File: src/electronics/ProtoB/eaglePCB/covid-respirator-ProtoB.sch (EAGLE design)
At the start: 49 parts, among them IC1 AD825R, IC2 L7805CV-DG, IC3 AD8607R, IC4 AD8607R, T2 BC548

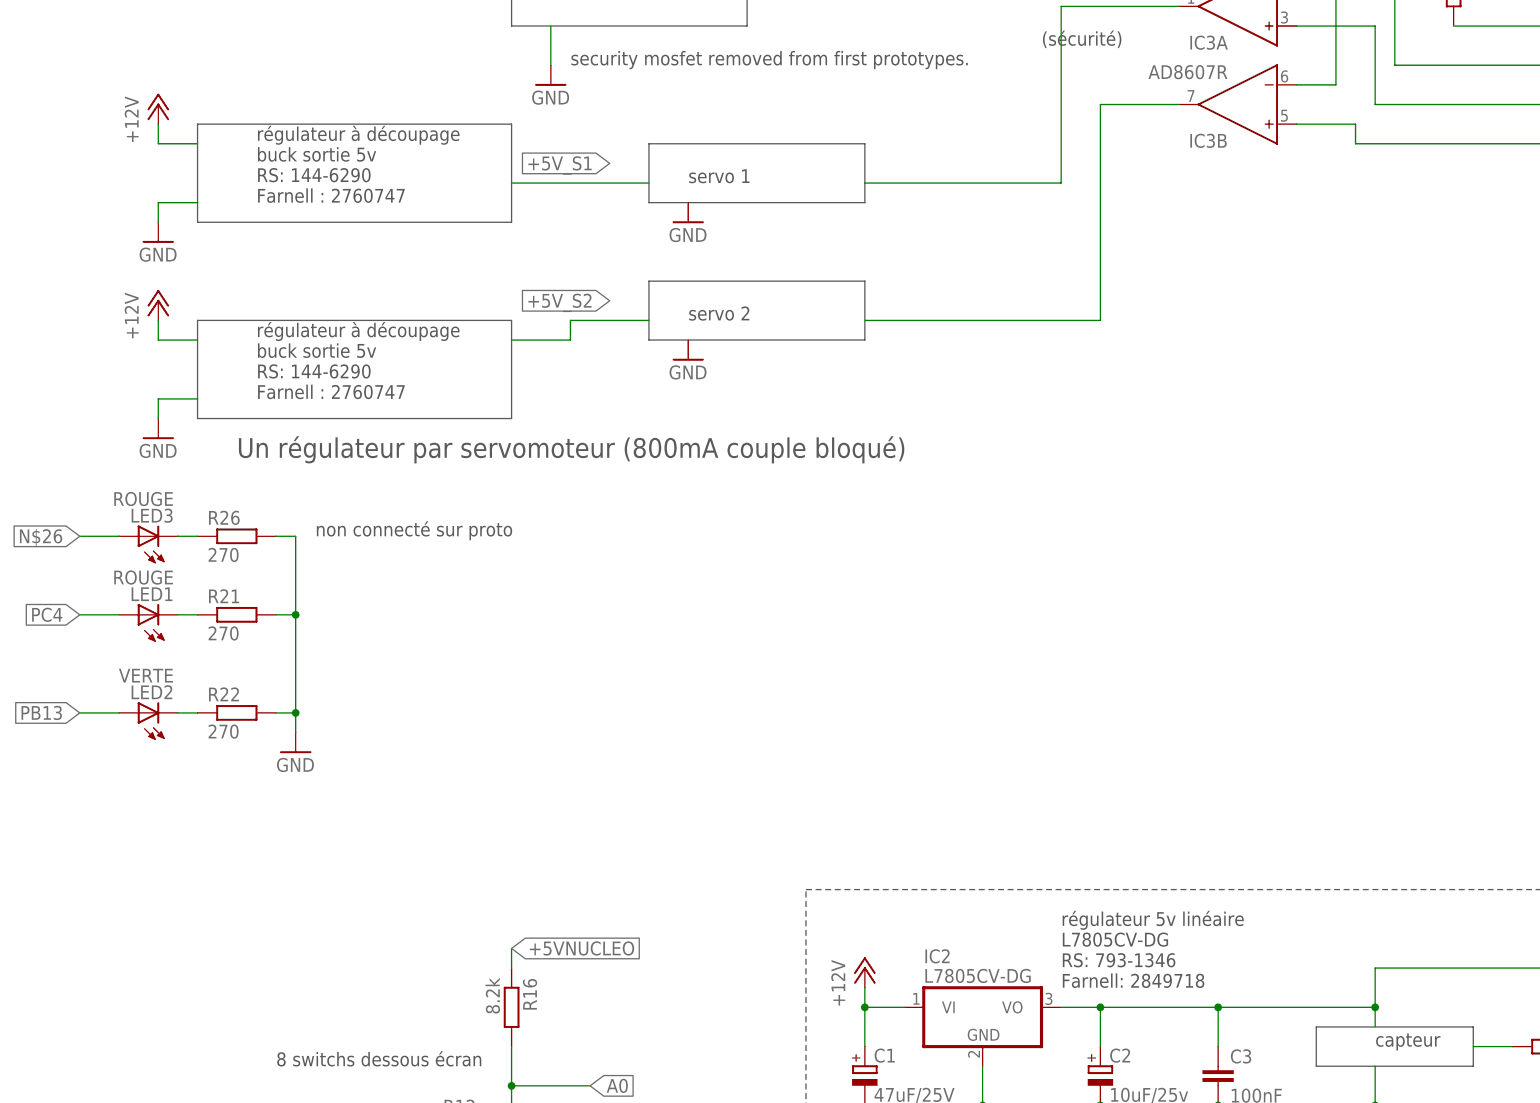
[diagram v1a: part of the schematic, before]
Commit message: update protoB schematic
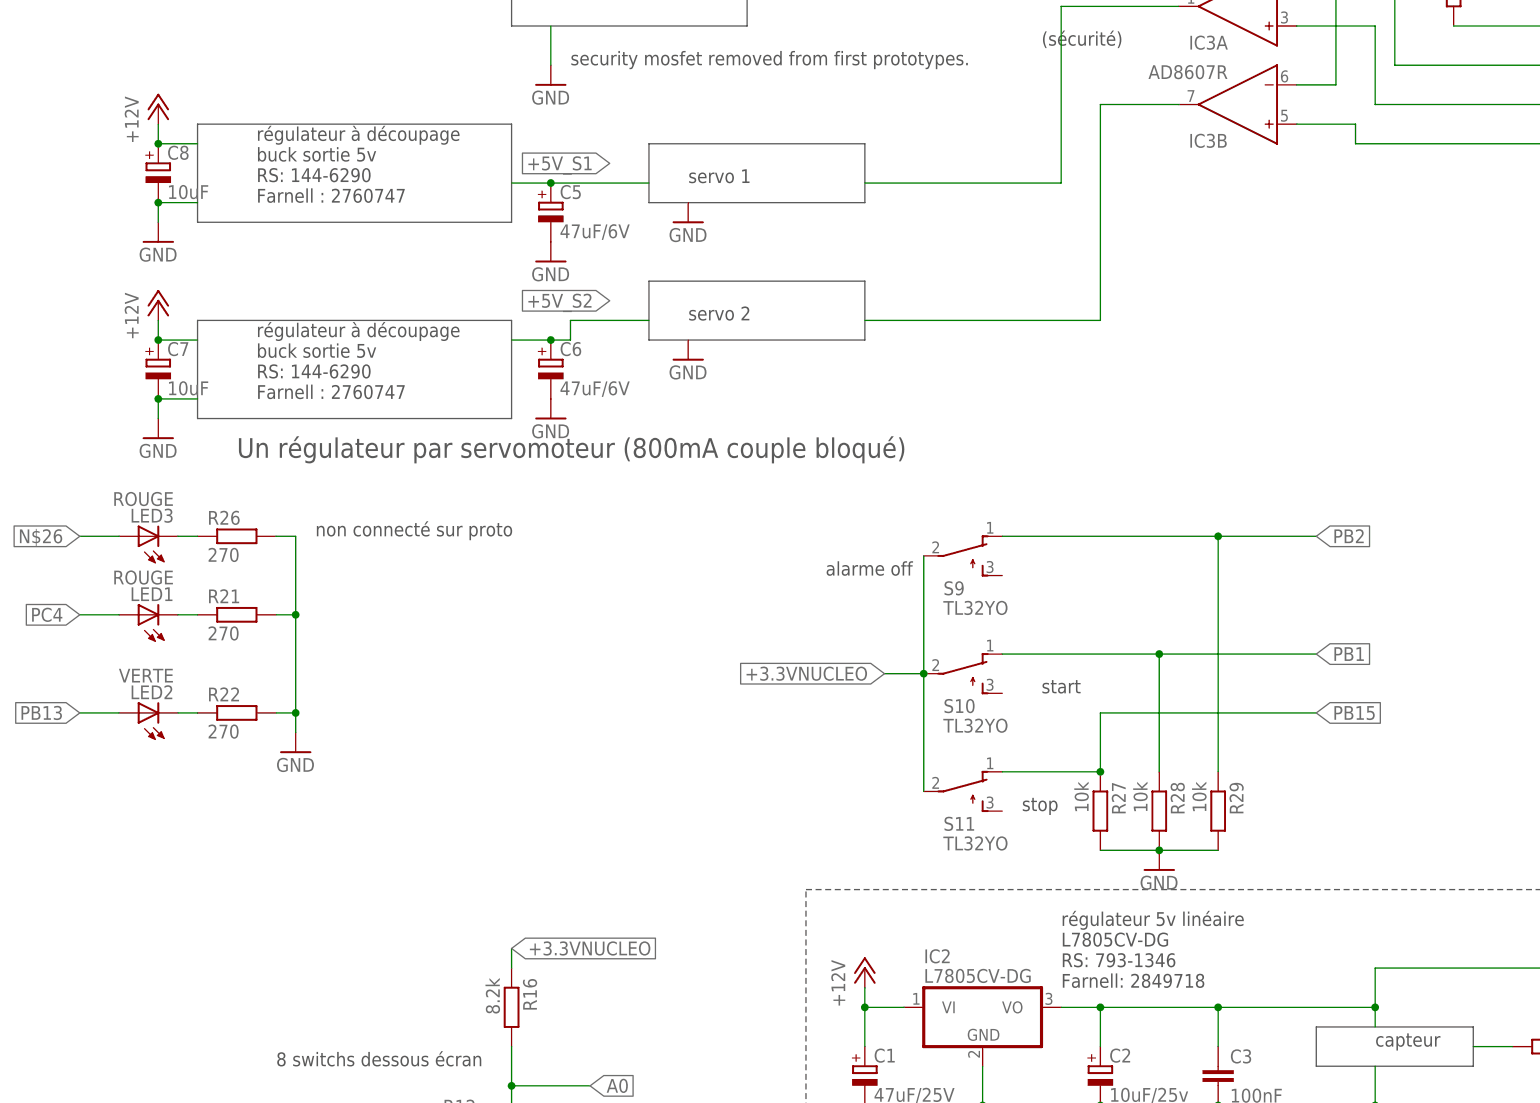
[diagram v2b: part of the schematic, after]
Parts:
- added C5, C6: 47uF/6V, rcl:CPOL-EU150CLZ-1010
- added C7, C8: 10uF, rcl:CPOL-EU150CLZ-1010
- added R27, R28, R29: 10k, rcl:R-EU_0207/10
- added S10, S11, S9: TL32YO, switch:TL32YO
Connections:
- new net +3.3VNUCLEO: R16.1, S10.P, S11.P, S9.P
- new net +5V_S1: C5.+
- new net +5V_S2: C6.+
- new net PB1: R28.1, S10.O
- new net PB15: R27.1, S11.O
- new net PB2: R29.1, S9.O
- net +12V: now also C7.+, C8.+
- net +5VNUCLEO: no longer R16.1
- net GND: now also C5.-, C6.-, C7.-, C8.-, R27.2, R28.2, R29.2
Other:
- note added: "alarme off"
- note added: "start"
- note added: "stop"
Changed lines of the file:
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@@
 <part name="LED3" library="led" deviceset="LED" device="3MM" value="ROUGE"/>
 <part name="R26" library="rcl" deviceset="R-EU_" device="0207/10" value="270"/>
+<part name="C5" library="rcl" deviceset="CPOL-EU" device="150CLZ-1010" value="47uF/6V"/>
+<part name="C6" library="rcl" deviceset="CPOL-EU" device="150CLZ-1010" value="47uF/6V"/>
+<part name="GND16" library="supply1" deviceset="GND" device=""/>
+<part name="GND17" library="supply1" deviceset="GND" device=""/>
+<part name="C7" library="rcl" deviceset="CPOL-EU" device="150CLZ-1010" value="10uF"/>
+<part name="C8" library="rcl" deviceset="CPOL-EU" device="150CLZ-1010" value="10uF"/>
+<part name="S9" library="switch" deviceset="TL32YO" device=""/>
+<part name="S10" library="switch" deviceset="TL32YO" device=""/>
+<part name="S11" library="switch" deviceset="TL32YO" device=""/>
+<part name="R27" library="rcl" deviceset="R-EU_" device="0207/10" value="10k"/>
+<part name="R28" library="rcl" deviceset="R-EU_" device="0207/10" value="10k"/>
+<part name="R29" library="rcl" deviceset="R-EU_" device="0207/10" value="10k"/>
+<part name="GND18" library="supply1" deviceset="GND" device=""/>
 </parts>
 <sheets>
@@
 pour un pont diviseur fixé</text>
 <text x="58.42" y="35.56" size="1.778" layer="97">non connecté sur proto</text>
+<text x="124.46" y="30.48" size="1.778" layer="97">alarme off</text>
+<text x="152.4" y="15.24" size="1.778" layer="97">start</text>
+<text x="149.86" y="0" size="1.778" layer="97">stop</text>
 </plain>
 <instances>
@@
 <instance part="LED3" gate="G$1" x="35.56" y="35.56" rot="R90"/>
 <instance part="R26" gate="G$1" x="48.26" y="35.56"/>
+<instance part="C5" gate="G$1" x="88.9" y="78.74"/>
+<instance part="C6" gate="G$1" x="88.9" y="58.42"/>
+<instance part="GND16" gate="1" x="88.9" y="50.8"/>
+<instance part="GND17" gate="1" x="88.9" y="71.12"/>
+<instance part="C7" gate="G$1" x="38.1" y="58.42"/>
+<instance part="C8" gate="G$1" x="38.1" y="83.82"/>
+<instance part="S9" gate="BEF1" x="142.24" y="33.02" rot="R270"/>
+<instance part="S10" gate="BEF1" x="142.24" y="17.78" rot="R270"/>
+<instance part="S11" gate="BEF1" x="142.24" y="2.54" rot="R270"/>
+<instance part="R27" gate="G$1" x="160.02" y="0" rot="R270"/>
+<instance part="R28" gate="G$1" x="167.64" y="0" rot="R270"/>
+<instance part="R29" gate="G$1" x="175.26" y="0" rot="R270"/>
+<instance part="GND18" gate="1" x="167.64" y="-7.62"/>
 </instances>
 <busses>
@@
 <wire x1="43.18" y1="78.74" x2="38.1" y2="78.74" width="0.1524" layer="91"/>
 <wire x1="38.1" y1="78.74" x2="38.1" y2="76.2" width="0.1524" layer="91"/>
+<pinref part="C8" gate="G$1" pin="-"/>
+<junction x="38.1" y="78.74"/>
 </segment>
 <segment>
@@
 <wire x1="43.18" y1="53.34" x2="38.1" y2="53.34" width="0.1524" layer="91"/>
 <wire x1="38.1" y1="53.34" x2="38.1" y2="50.8" width="0.1524" layer="91"/>
+<pinref part="C7" gate="G$1" pin="-"/>
+<junction x="38.1" y="53.34"/>
 </segment>
 <segment>
@@
 <wire x1="246.38" y1="71.12" x2="246.38" y2="68.58" width="0.1524" layer="91"/>
 </segment>
+<segment>
+<pinref part="C6" gate="G$1" pin="-"/>
+<pinref part="GND16" gate="1" pin="GND"/>
+</segment>
+<segment>
+<pinref part="C5" gate="G$1" pin="-"/>
+<pinref part="GND17" gate="1" pin="GND"/>
+</segment>
+<segment>
+<pinref part="R28" gate="G$1" pin="2"/>
+<pinref part="GND18" gate="1" pin="GND"/>
+<pinref part="R27" gate="G$1" pin="2"/>
+<wire x1="160.02" y1="-5.08" x2="167.64" y2="-5.08" width="0.1524" layer="91"/>
+<junction x="167.64" y="-5.08"/>
+<pinref part="R29" gate="G$1" pin="2"/>
+<wire x1="167.64" y1="-5.08" x2="175.26" y2="-5.08" width="0.1524" layer="91"/>
+</segment>
 </net>
 <net name="+12V" class="0">
@@
 <wire x1="38.1" y1="88.9" x2="38.1" y2="86.36" width="0.1524" layer="91"/>
 <wire x1="38.1" y1="86.36" x2="43.18" y2="86.36" width="0.1524" layer="91"/>
+<pinref part="C8" gate="G$1" pin="+"/>
+<junction x="38.1" y="86.36"/>
 </segment>
 <segment>
@@
 <wire x1="38.1" y1="63.5" x2="38.1" y2="60.96" width="0.1524" layer="91"/>
 <wire x1="38.1" y1="60.96" x2="43.18" y2="60.96" width="0.1524" layer="91"/>
+<pinref part="C7" gate="G$1" pin="+"/>
+<junction x="38.1" y="60.96"/>
 </segment>
 </net>
@@
 <wire x1="101.6" y1="63.5" x2="91.44" y2="63.5" width="0.1524" layer="91"/>
 <wire x1="91.44" y1="63.5" x2="91.44" y2="60.96" width="0.1524" layer="91"/>
-<wire x1="91.44" y1="60.96" x2="83.82" y2="60.96" width="0.1524" layer="91"/>
+<wire x1="91.44" y1="60.96" x2="88.9" y2="60.96" width="0.1524" layer="91"/>
+<pinref part="C6" gate="G$1" pin="+"/>
+<wire x1="88.9" y1="60.96" x2="83.82" y2="60.96" width="0.1524" layer="91"/>
+<junction x="88.9" y="60.96"/>
 </segment>
 </net>
@@
 <segment>
 <label x="96.52" y="83.82" size="1.778" layer="95" rot="R180" xref="yes"/>
-<wire x1="101.6" y1="81.28" x2="83.82" y2="81.28" width="0.1524" layer="91"/>
+<wire x1="101.6" y1="81.28" x2="88.9" y2="81.28" width="0.1524" layer="91"/>
+<pinref part="C5" gate="G$1" pin="+"/>
+<wire x1="88.9" y1="81.28" x2="83.82" y2="81.28" width="0.1524" layer="91"/>
+<junction x="88.9" y="81.28"/>
 </segment>
 </net>
@@
 <wire x1="-22.86" y1="-17.78" x2="-27.94" y2="-17.78" width="0.1524" layer="91"/>
 <junction x="-22.86" y="-17.78"/>
-</segment>
-<segment>
-<pinref part="R16" gate="G$1" pin="1"/>
-<wire x1="83.82" y1="-20.32" x2="83.82" y2="-17.78" width="0.1524" layer="91"/>
-<label x="83.82" y="-17.78" size="1.778" layer="95" xref="yes"/>
 </segment>
 </net>
@@
 </segment>
 </net>
+<net name="PB15" class="0">
+<segment>
+<pinref part="R27" gate="G$1" pin="1"/>
+<pinref part="S11" gate="BEF1" pin="O"/>
+<wire x1="160.02" y1="5.08" x2="147.32" y2="5.08" width="0.1524" layer="91"/>
+<wire x1="160.02" y1="5.08" x2="160.02" y2="12.7" width="0.1524" layer="91"/>
+<junction x="160.02" y="5.08"/>
+<wire x1="160.02" y1="12.7" x2="187.96" y2="12.7" width="0.1524" layer="91"/>
+<label x="187.96" y="12.7" size="1.778" layer="95" xref="yes"/>
+</segment>
+</net>
+<net name="PB1" class="0">
+<segment>
+<pinref part="R28" gate="G$1" pin="1"/>
+<pinref part="S10" gate="BEF1" pin="O"/>
+<wire x1="167.64" y1="5.08" x2="167.64" y2="20.32" width="0.1524" layer="91"/>
+<wire x1="167.64" y1="20.32" x2="147.32" y2="20.32" width="0.1524" layer="91"/>
+<wire x1="167.64" y1="20.32" x2="187.96" y2="20.32" width="0.1524" layer="91"/>
+<junction x="167.64" y="20.32"/>
+<label x="187.96" y="20.32" size="1.778" layer="95" xref="yes"/>
+</segment>
+</net>
+<net name="PB2" class="0">
+<segment>
+<pinref part="R29" gate="G$1" pin="1"/>
+<pinref part="S9" gate="BEF1" pin="O"/>
+<wire x1="175.26" y1="5.08" x2="175.26" y2="35.56" width="0.1524" layer="91"/>
+<wire x1="175.26" y1="35.56" x2="147.32" y2="35.56" width="0.1524" layer="91"/>
+<wire x1="175.26" y1="35.56" x2="187.96" y2="35.56" width="0.1524" layer="91"/>
+<junction x="175.26" y="35.56"/>
+<label x="187.96" y="35.56" size="1.778" layer="95" xref="yes"/>
+</segment>
+</net>
+<net name="+3.3VNUCLEO" class="0">
+<segment>
+<pinref part="R16" gate="G$1" pin="1"/>
+<wire x1="83.82" y1="-20.32" x2="83.82" y2="-17.78" width="0.1524" layer="91"/>
+<label x="83.82" y="-17.78" size="1.778" layer="95" xref="yes"/>
+</segment>
+<segment>
+<pinref part="S9" gate="BEF1" pin="P"/>
+<pinref part="S10" gate="BEF1" pin="P"/>
+<wire x1="137.16" y1="33.02" x2="137.16" y2="17.78" width="0.1524" layer="91"/>
+<pinref part="S11" gate="BEF1" pin="P"/>
+<wire x1="137.16" y1="17.78" x2="137.16" y2="2.54" width="0.1524" layer="91"/>
+<junction x="137.16" y="17.78"/>
+<wire x1="137.16" y1="17.78" x2="132.08" y2="17.78" width="0.1524" layer="91"/>
+<label x="132.08" y="17.78" size="1.778" layer="95" rot="R180" xref="yes"/>
+</segment>
+</net>
